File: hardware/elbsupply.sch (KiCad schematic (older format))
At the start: 76 parts, among them CON1 AVR-ISP-6, IC1 ATMEGA8-AI, P1 OUT_POS, P2 OUT_GND, P3 POWER_IN, Q1 KST2907A, SW1 SW_L, SW2 SW_R, U1 LM393, U2 TPS54331DDA, U3 LT1490, U4 LM358, U5 TS78L05CS, U6 LT3083

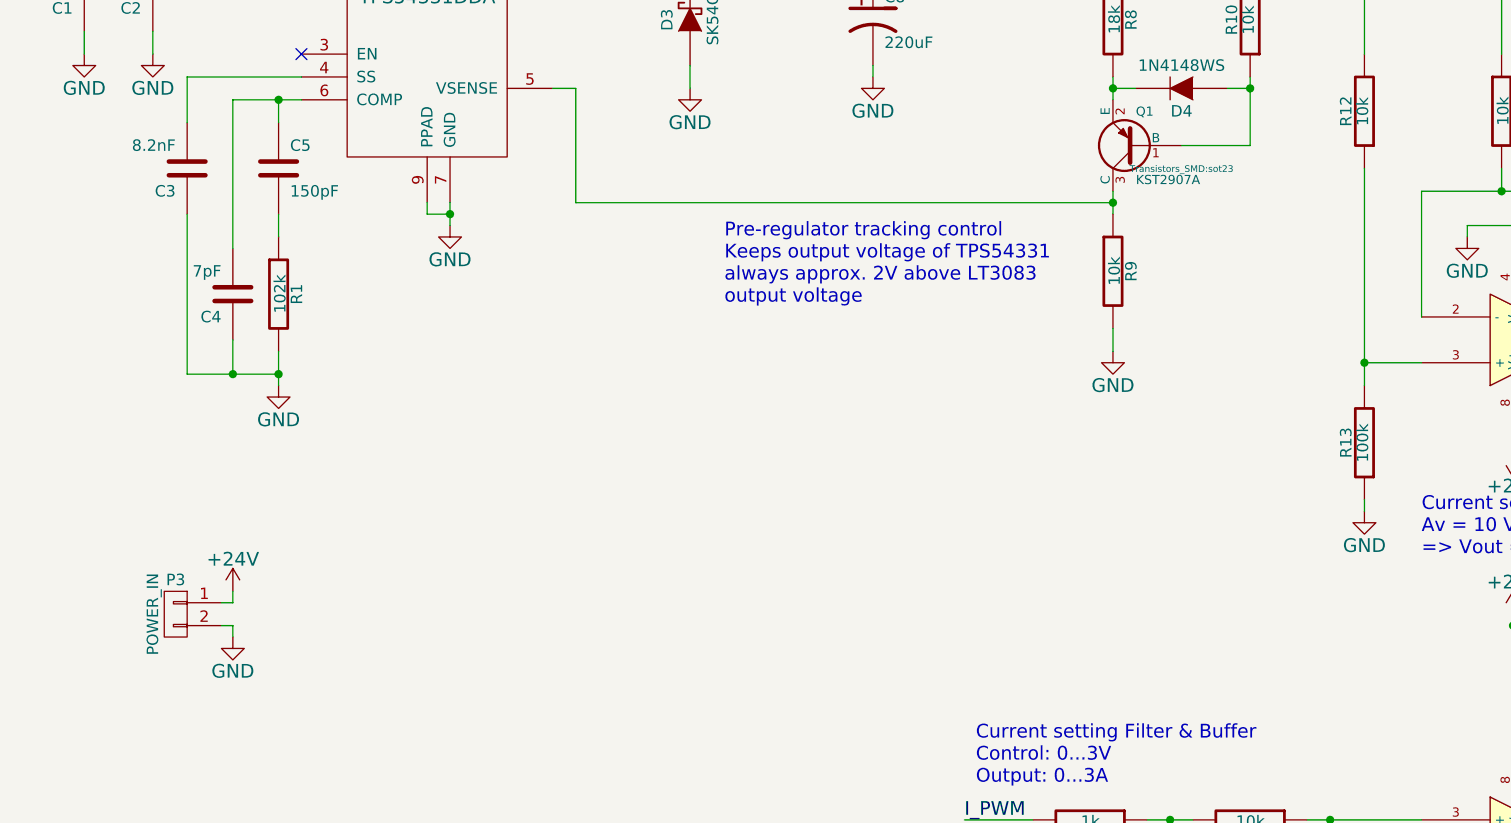
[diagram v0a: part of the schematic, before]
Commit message: fixed Q1 footprint issues
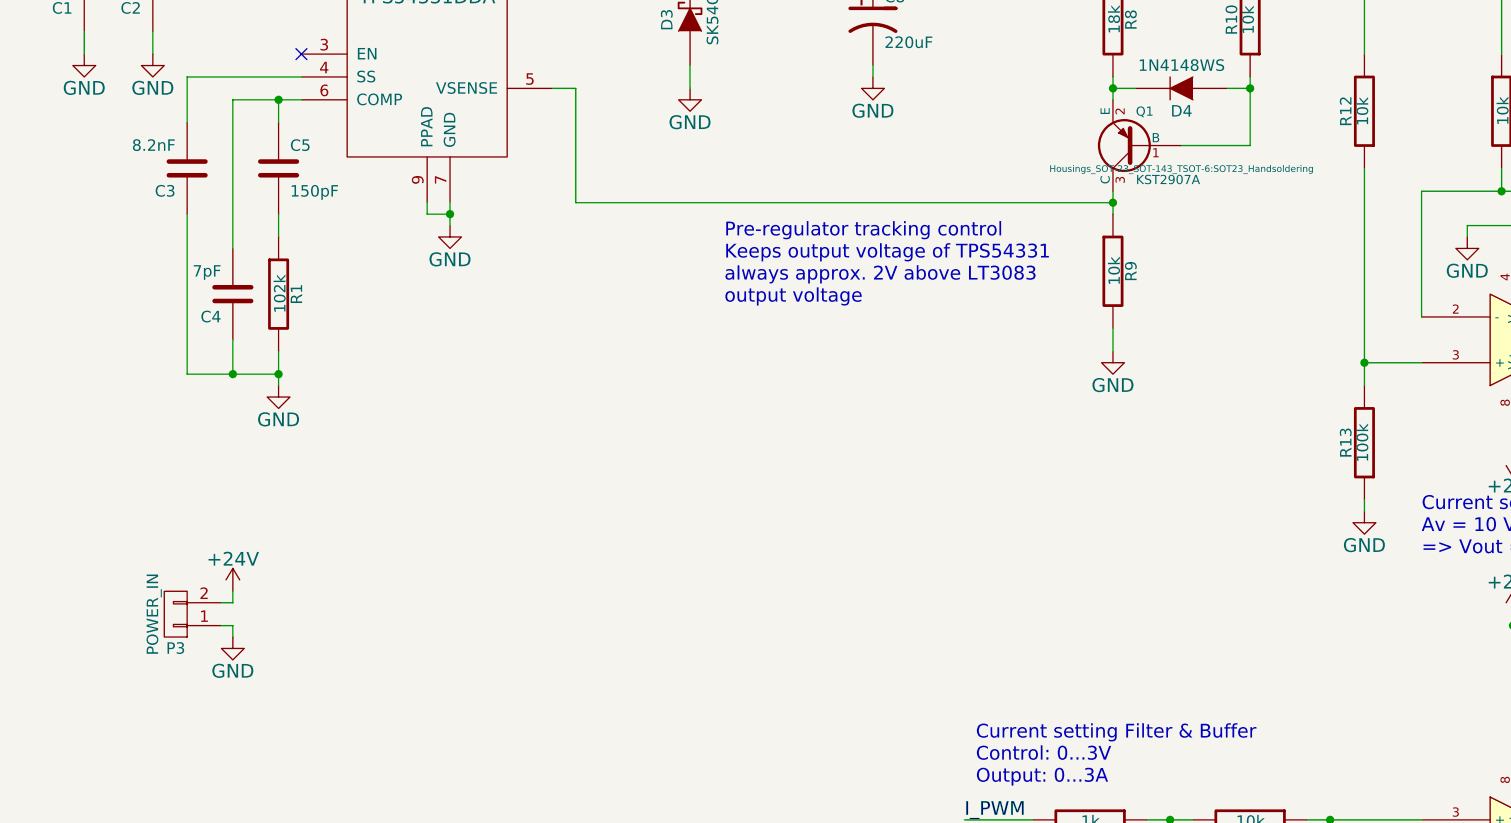
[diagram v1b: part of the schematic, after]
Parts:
- Q1: footprint Transistors_SMD:sot23 -> Housings_SOT-23_SOT-143_TSOT-6:SOT23_Handsoldering
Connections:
- net +24V: now also P3.2 (P2); no longer P3.1 (P1)
- net GND: now also P3.1 (P1); no longer P3.2 (P2)
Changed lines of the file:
@@
 F 0 "Q1" H 5400 2101 40  0000 R CNN
 F 1 "KST2907A" H 5400 2400 40  0000 R CNN
-F 2 "Transistors_SMD:sot23" H 5200 2352 29  0000 C CNN
+F 2 "Housings_SOT-23_SOT-143_TSOT-6:SOT23_Handsoldering" H 5200 2352 29  0000 C CNN
 F 3 "" H 5400 2250 60  0000 C CNN
 	1    5400 2250
@@
 F 3 "" H 1200 4300 60  0000 C CNN
 	1    1200 4300
-	-1   0    0    -1
+	-1   0    0    1
 $EndComp
 $Comp

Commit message: continued layout
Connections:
- net LIN_OUT: now reaches C26.1, D5.1, P1.1 (P1), R10.2, RP4.1 (P1), U6.3 (OUT)
- net LIN_IN: now reaches C20.1, R15.1, R17.1, U6.4 (Vcontrol), U6.5 (IN)
- net SMPS_OUT: now reaches C8.1, L1.2, R12.2, R15.2, R8.1
- net SMPS_SW: now reaches C6.2, D3.2 (K), L1.1, U2.8 (PH)
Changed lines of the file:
@@
 Wire Wire Line
 	1450 4250 1400 4250
+Text Label 4250 1400 0    60   ~ 0
+SMPS_OUT
+Text Label 2850 1400 0    60   ~ 0
+SMPS_SW
+Text Label 11850 1400 0    60   ~ 0
+LIN_OUT
+Text Label 7050 1400 0    60   ~ 0
+LIN_IN
 $EndSCHEMATC

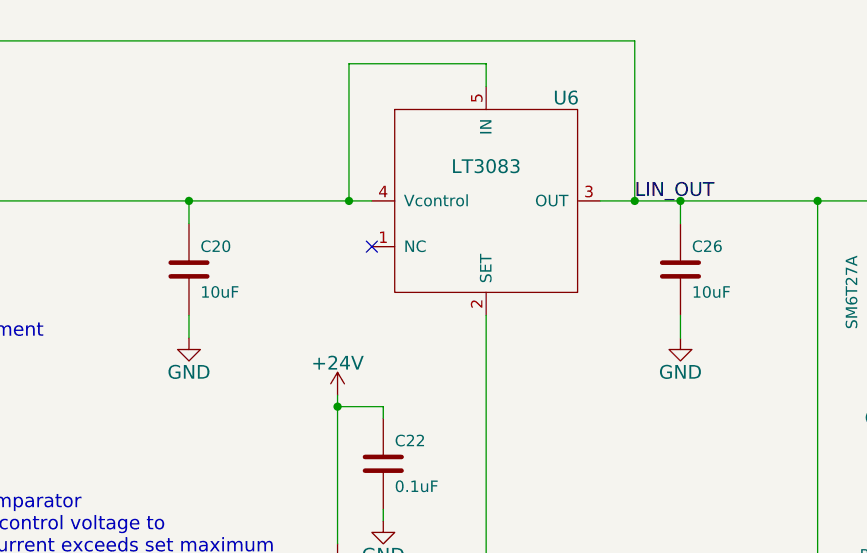
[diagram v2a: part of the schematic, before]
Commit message: LT3083 output capacitors exchanged for electrolytics
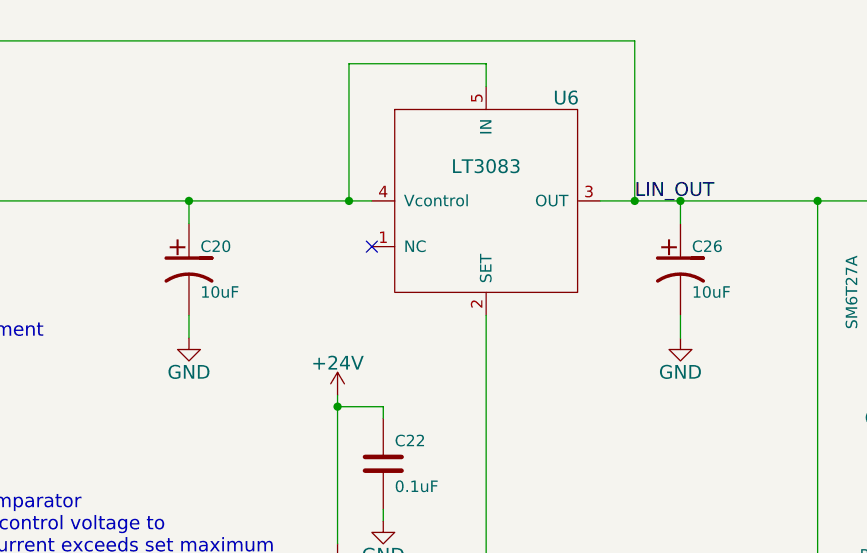
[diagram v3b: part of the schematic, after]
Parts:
- removed C20, C26: 10uF, Capacitors_SMD:C_0603_HandSoldering, symbol C
- added C20, C26: 10uF, symbol CP1
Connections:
- net GND: now also C20.2, C26.2
- net LIN_IN: now also C20.1
- net LIN_OUT: now also C26.1
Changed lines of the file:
@@
 I_ADC
-$Comp
-L C C26
-U 1 1 54E3DA6D
-P 12050 1700
-F 0 "C26" H 12100 1800 50  0000 L CNN
-F 1 "10uF" H 12100 1600 50  0000 L CNN
-F 2 "Capacitors_SMD:C_0603_HandSoldering" H 12088 1550 30  0001 C CNN
-F 3 "" H 12050 1700 60  0000 C CNN
-	1    12050 1700
-	1    0    0    -1
-$EndComp
 $Comp
 L GND #PWR017
@@
 F 3 "" H 12050 2000 60  0000 C CNN
 	1    12050 2000
-	1    0    0    -1
-$EndComp
-$Comp
-L C C20
-U 1 1 54E3DDBB
-P 9900 1700
-F 0 "C20" H 9950 1800 50  0000 L CNN
-F 1 "10uF" H 9950 1600 50  0000 L CNN
-F 2 "Capacitors_SMD:C_0603_HandSoldering" H 9938 1550 30  0001 C CNN
-F 3 "" H 9900 1700 60  0000 C CNN
-	1    9900 1700
 	1    0    0    -1
 $EndComp
@@
 Text Label 7050 1400 0    60   ~ 0
 LIN_IN
+$Comp
+L CP1 C20
+U 1 1 54FC21B2
+P 9900 1700
+F 0 "C20" H 9950 1800 50  0000 L CNN
+F 1 "10uF" H 9950 1600 50  0000 L CNN
+F 2 "" H 9900 1700 60  0000 C CNN
+F 3 "" H 9900 1700 60  0000 C CNN
+	1    9900 1700
+	1    0    0    -1
+$EndComp
+$Comp
+L CP1 C26
+U 1 1 54FC2BFC
+P 12050 1700
+F 0 "C26" H 12100 1800 50  0000 L CNN
+F 1 "10uF" H 12100 1600 50  0000 L CNN
+F 2 "" H 12050 1700 60  0000 C CNN
+F 3 "" H 12050 1700 60  0000 C CNN
+	1    12050 1700
+	1    0    0    -1
+$EndComp
 $EndSCHEMATC

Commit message: rev. A routing finished
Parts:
- C20, C26: footprint (none) -> Capacitors_SMD:c_elec_4x4.5
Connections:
- net ENC_A: now also IC1.2 ((XCK/T0)PD4); no longer IC1.1 ((INT1)PD3)
- net ENC_B: now also IC1.1 ((INT1)PD3); no longer IC1.2 ((XCK/T0)PD4)
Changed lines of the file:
@@
 Text Label 14150 8800 2    60   ~ 0
 ENC_SW
+Text Label 14150 9000 2    60   ~ 0
+ENC_A
 Text Label 14150 8900 2    60   ~ 0
-ENC_A
-Text Label 14150 9000 2    60   ~ 0
 ENC_B
 Text Label 6500 9750 2    60   ~ 0
@@
 F 0 "C20" H 9950 1800 50  0000 L CNN
 F 1 "10uF" H 9950 1600 50  0000 L CNN
-F 2 "" H 9900 1700 60  0000 C CNN
+F 2 "Capacitors_SMD:c_elec_4x4.5" H 9900 1700 60  0001 C CNN
 F 3 "" H 9900 1700 60  0000 C CNN
 	1    9900 1700
@@
 F 0 "C26" H 12100 1800 50  0000 L CNN
 F 1 "10uF" H 12100 1600 50  0000 L CNN
-F 2 "" H 12050 1700 60  0000 C CNN
+F 2 "Capacitors_SMD:c_elec_4x4.5" H 12050 1700 60  0001 C CNN
 F 3 "" H 12050 1700 60  0000 C CNN
 	1    12050 1700

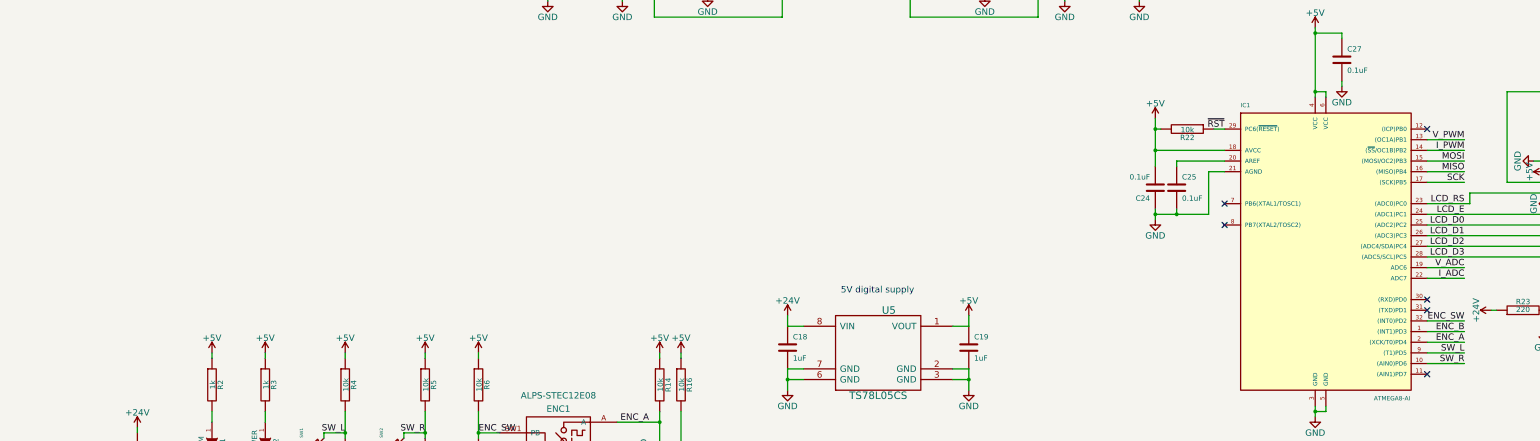
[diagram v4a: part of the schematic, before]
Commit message: added two more switches for cleaner UI
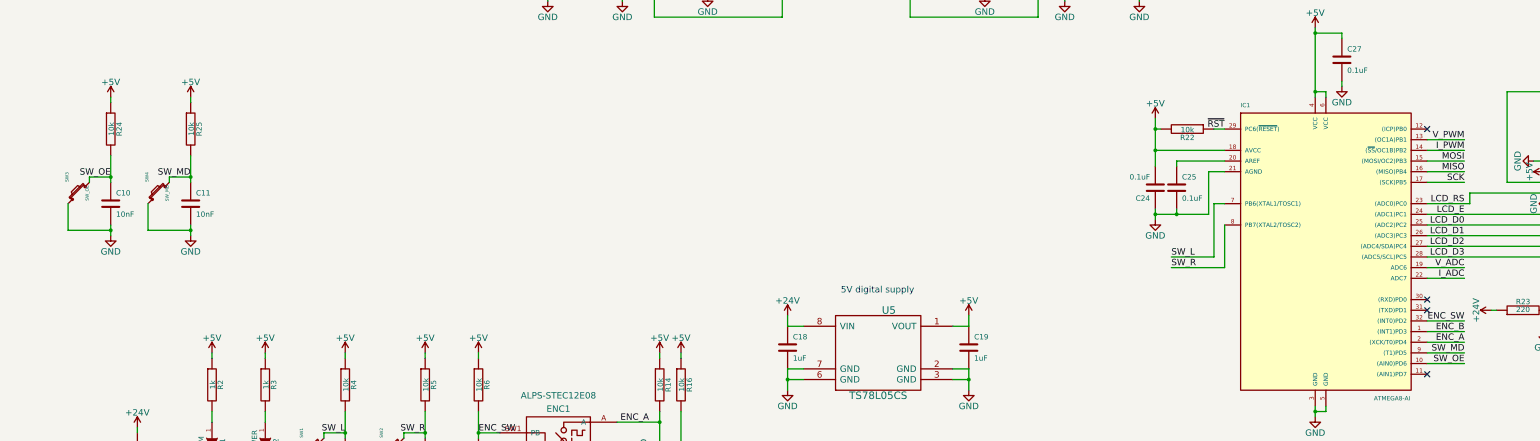
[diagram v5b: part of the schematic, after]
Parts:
- added C10, C11: 10nF, Capacitors_SMD:C_0603_HandSoldering, symbol C
- added R24, R25: 10k, Resistors_SMD:R_0603_HandSoldering, symbol R
- added SW3: SW_OE, devthrash_KICAD:Button-SMT-standard, symbol SW_PUSH_SMALL
- added SW4: SW_MD, devthrash_KICAD:Button-SMT-standard, symbol SW_PUSH_SMALL
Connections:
- net +5V: now also R24.1, R25.1
- net GND: now also C10.2, C11.2, SW3.1, SW4.1
- net SW_L: now also IC1.7 (PB6(XTAL1/TOSC1)); no longer IC1.9 ((T1)PD5)
- net SW_R: now also IC1.8 (PB7(XTAL2/TOSC2)); no longer IC1.10 ((AIN0)PD6)
- new net SW_MD: C11.1, IC1.9 ((T1)PD5), R25.2, SW4.2
- new net SW_OE: C10.1, IC1.10 ((AIN0)PD6), R24.2, SW3.2
- no-connect marks 16 -> 14
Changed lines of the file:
@@
 	1    0    0    -1
 $EndComp
-NoConn ~ 11900 7700
-NoConn ~ 11900 7900
 $Comp
 L C C27
@@
 NoConn ~ 7850 1750
 NoConn ~ 7850 1850
-Text Label 14150 9100 2    60   ~ 0
+Text Label 11400 8200 0    60   ~ 0
 SW_L
-Text Label 14150 9200 2    60   ~ 0
+Text Label 11400 8300 0    60   ~ 0
 SW_R
 $Comp
@@
 	1    0    0    -1
 $EndComp
+Wire Wire Line
+	11900 7700 11800 7700
+Wire Wire Line
+	11800 7700 11800 8200
+Wire Wire Line
+	11800 8200 11400 8200
+Wire Wire Line
+	11900 7900 11900 8300
+Wire Wire Line
+	11900 8300 11400 8300
+$Comp
+L SW_PUSH_SMALL SW3
+U 1 1 54FC72BC
+P 1150 7600
+F 0 "SW3" H 1300 7710 30  0000 C CNN
+F 1 "SW_OE" H 1150 7521 30  0000 C CNN
+F 2 "devthrash_KICAD:Button-SMT-standard" H 1150 7600 60  0001 C CNN
+F 3 "" H 1150 7600 60  0000 C CNN
+	1    1150 7600
+	0    -1   -1   0
+$EndComp
+$Comp
+L C C10
+U 1 1 54FC72C2
+P 1450 7700
+F 0 "C10" H 1500 7800 50  0000 L CNN
+F 1 "10nF" H 1500 7600 50  0000 L CNN
+F 2 "Capacitors_SMD:C_0603_HandSoldering" H 1488 7550 30  0001 C CNN
+F 3 "" H 1450 7700 60  0000 C CNN
+	1    1450 7700
+	1    0    0    -1
+$EndComp
+$Comp
+L GND #PWR070
+U 1 1 54FC72C8
+P 1450 8000
+F 0 "#PWR070" H 1450 7750 60  0001 C CNN
+F 1 "GND" H 1450 7850 60  0000 C CNN
+F 2 "" H 1450 8000 60  0000 C CNN
+F 3 "" H 1450 8000 60  0000 C CNN
+	1    1450 8000
+	1    0    0    -1
+$EndComp
+$Comp
+L R R24
+U 1 1 54FC72CE
+P 1450 7000
+F 0 "R24" V 1530 7000 50  0000 C CNN
+F 1 "10k" V 1457 7001 50  0000 C CNN
+F 2 "Resistors_SMD:R_0603_HandSoldering" V 1380 7000 30  0001 C CNN
+F 3 "" H 1450 7000 30  0000 C CNN
+	1    1450 7000
+	1    0    0    -1
+$EndComp
+$Comp
+L +5V #PWR071
+U 1 1 54FC72D4
+P 1450 6700
+F 0 "#PWR071" H 1450 6550 60  0001 C CNN
+F 1 "+5V" H 1450 6840 60  0000 C CNN
+F 2 "" H 1450 6700 60  0000 C CNN
+F 3 "" H 1450 6700 60  0000 C CNN
+	1    1450 6700
+	1    0    0    -1
+$EndComp
+Text Label 1450 7450 2    60   ~ 0
+SW_OE
+$Comp
+L SW_PUSH_SMALL SW4
+U 1 1 54FC72DB
+P 1900 7600
+F 0 "SW4" H 2050 7710 30  0000 C CNN
+F 1 "SW_MD" H 1900 7521 30  0000 C CNN
+F 2 "devthrash_KICAD:Button-SMT-standard" H 1900 7600 60  0001 C CNN
+F 3 "" H 1900 7600 60  0000 C CNN
+	1    1900 7600
+	0    -1   -1   0
+$EndComp
+$Comp
+L C C11
+U 1 1 54FC72E1
+P 2200 7700
+F 0 "C11" H 2250 7800 50  0000 L CNN
+F 1 "10nF" H 2250 7600 50  0000 L CNN
+F 2 "Capacitors_SMD:C_0603_HandSoldering" H 2238 7550 30  0001 C CNN
+F 3 "" H 2200 7700 60  0000 C CNN
+	1    2200 7700
+	1    0    0    -1
+$EndComp
+$Comp
+L GND #PWR072
+U 1 1 54FC72E7
+P 2200 8000
+F 0 "#PWR072" H 2200 7750 60  0001 C CNN
+F 1 "GND" H 2200 7850 60  0000 C CNN
+F 2 "" H 2200 8000 60  0000 C CNN
+F 3 "" H 2200 8000 60  0000 C CNN
+	1    2200 8000
+	1    0    0    -1
+$EndComp
+$Comp
+L R R25
+U 1 1 54FC72ED
+P 2200 7000
+F 0 "R25" V 2280 7000 50  0000 C CNN
+F 1 "10k" V 2207 7001 50  0000 C CNN
+F 2 "Resistors_SMD:R_0603_HandSoldering" V 2130 7000 30  0001 C CNN
+F 3 "" H 2200 7000 30  0000 C CNN
+	1    2200 7000
+	1    0    0    -1
+$EndComp
+$Comp
+L +5V #PWR073
+U 1 1 54FC72F3
+P 2200 6700
+F 0 "#PWR073" H 2200 6550 60  0001 C CNN
+F 1 "+5V" H 2200 6840 60  0000 C CNN
+F 2 "" H 2200 6700 60  0000 C CNN
+F 3 "" H 2200 6700 60  0000 C CNN
+	1    2200 6700
+	1    0    0    -1
+$EndComp
+Text Label 2200 7450 2    60   ~ 0
+SW_MD
+Wire Wire Line
+	1450 7900 1450 8000
+Wire Wire Line
+	1450 7950 1050 7950
+Wire Wire Line
+	1050 7950 1050 7700
+Connection ~ 1450 7950
+Wire Wire Line
+	1250 7500 1250 7450
+Wire Wire Line
+	1250 7450 1450 7450
+Wire Wire Line
+	1450 7250 1450 7500
+Connection ~ 1450 7450
+Wire Wire Line
+	1450 6700 1450 6750
+Wire Wire Line
+	2200 7900 2200 8000
+Wire Wire Line
+	2200 7950 1800 7950
+Wire Wire Line
+	1800 7950 1800 7700
+Connection ~ 2200 7950
+Wire Wire Line
+	2000 7500 2000 7450
+Wire Wire Line
+	2000 7450 2200 7450
+Wire Wire Line
+	2200 7250 2200 7500
+Connection ~ 2200 7450
+Wire Wire Line
+	2200 6700 2200 6750
+Text Label 14150 9100 2    60   ~ 0
+SW_MD
+Text Label 14150 9200 2    60   ~ 0
+SW_OE
 $EndSCHEMATC
